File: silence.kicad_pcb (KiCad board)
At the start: 2 copper layers, 134 parts, among them J1 15EDGVC-3.81-02P, J2 15EDGVC-2.5-04P-14, J3 DEBUG, J4 15EDGVC-3.81-03P, J5 15EDGVC-3.81-02P, J6 EXTRA, J7 15EDGVC-3.81-03P, Q1 AO3400A, Q2 AO3400A, Q3 AO3400A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

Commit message: Minor updates
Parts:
- removed C13, C14, C15, C16, C17, C18, C19: 10u, Capacitor_SMD:C_1206_3216Metric
- added C6: 100u (EEEFTH101XAP), Capacitor_SMD:CP_Elec_6.3x7.7, F.Cu at (196.5, 62.7)
- added R47: 0, Resistor_SMD:R_0603_1608Metric, F.Cu at (213.0, 116.7)
- moved C21 345.3 mm to (276.2, 77.1)
- moved C23 345.3 mm to (276.2, 79.6)
- moved C24 345.3 mm to (276.2, 82.1)
- moved J6 345.3 mm to (279.9, 87.1)
- moved R26 345.3 mm to (276.2, 84.6)
- moved R27 345.3 mm to (276.2, 87.1)
- moved C22 345.3 mm to (285.7, 77.5)
- moved J3 345.3 mm to (280.6, 78.2)
- moved JP1 345.3 mm to (285.7, 81.0)
- moved SW1 345.3 mm to (265.7, 77.9)
- moved SW2 345.3 mm to (265.7, 86.4)
- moved U1 345.3 mm to (288.2, 64.8)
- moved C1 200.4 mm to (42.0, 22.8)
- moved C2 200.4 mm to (42.0, 25.3)
- moved C3 200.4 mm to (42.0, 27.8)
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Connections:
- FB2 pad 1: Net-(U8--) -> Net-(FB2-Pad1)
- R41 pad 1: Net-(U8-+) -> Net-(R41-Pad1)
- R41 pad 2: Net-(R41-Pad2) -> GND
- R42 pad 1: Net-(R41-Pad2) -> Net-(U8-+)
- R42 pad 2: GND -> Net-(R41-Pad1)
- U8 pad 4: Net-(U8--) -> Net-(FB2-Pad1)

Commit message: Routing almost finished
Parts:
- added C13: 10u, Capacitor_SMD:C_1206_3216Metric, F.Cu at (153.9, 66.0)
- added C14: 47u, Capacitor_SMD:C_1206_3216Metric, F.Cu at (153.9, 68.4)
- added D3: LED, LED_SMD:LED_0603_1608Metric, F.Cu at (173.1, 84.5)
- added D4: LED, LED_SMD:LED_0603_1608Metric, F.Cu at (173.1, 86.1)
- added D5: LED, LED_SMD:LED_0603_1608Metric, F.Cu at (166.3, 54.1)
- added JP3: WSEN, Jumper:SolderJumper-2_P1.3mm_Open_RoundedPad1.0x1.5mm, F.Cu at (191.9, 90.7)
- added JP4: WSEN, Jumper:SolderJumper-2_P1.3mm_Open_RoundedPad1.0x1.5mm, F.Cu at (191.9, 74.8)
- added L4: 4.7uH (SWPA5020S4R7MT), Inductor_SMD:L_Sunlord_SWPA5020S, F.Cu at (154.7, 62.0)
- added R48: 330, Resistor_SMD:R_0603_1608Metric, F.Cu at (153.1, 104.9)
- added R49: 330, Resistor_SMD:R_0603_1608Metric, F.Cu at (153.1, 101.9)
- added R50: 1, Resistor_SMD:R_0603_1608Metric, F.Cu at (150.8, 67.7)
- added R51: 10k, Resistor_SMD:R_0603_1608Metric, F.Cu at (170.0, 84.5)
- added R52: 10k, Resistor_SMD:R_0603_1608Metric, F.Cu at (170.0, 86.1)
- added R53: 47k, Resistor_SMD:R_0603_1608Metric, F.Cu at (163.3, 54.1)
- added kibuzzard-676F239E: G***, kibuzzard-676F239E, F.Cu at (149.9, 56.4)
- added kibuzzard-676F239E: G***, kibuzzard-676F239E, F.Cu at (199.8, 48.0)
- added kibuzzard-676F2404: G***, kibuzzard-676F2404, F.Cu at (149.9, 60.3)
- added kibuzzard-676F2404: G***, kibuzzard-676F2404, F.Cu at (201.0, 68.6)
- added kibuzzard-676F2425: G***, kibuzzard-676F2425, F.Cu at (150.5, 49.4)
- added kibuzzard-676F243D: G***, kibuzzard-676F243D, F.Cu at (195.7, 44.0)
- added kibuzzard-676F24DA: G***, kibuzzard-676F24DA, F.Cu at (203.6, 85.2)
- added kibuzzard-676F24FA: G***, kibuzzard-676F24FA, F.Cu at (197.6, 101.1)
- added kibuzzard-676F26EA: G***, kibuzzard-676F26EA, F.Cu at (161.0, 73.1)
- J6: footprint Connector_PinHeader_1.00mm:PinHeader_1x05_P1.00mm_Vertical -> Connector_PinHeader_2.54mm:PinHeader_1x05_P2.54mm_Vertical
- TP1, TP3: value DIN -> DO
- moved H3 245.9 mm to (203.9, 104.5)
- moved H1 225.6 mm to (203.9, 44.5)
- moved H4 192.5 mm to (143.9, 104.5)
- moved J2 174.8 mm to (150.7, 74.6), turned to 180 degrees
- moved H2 167.9 mm to (143.9, 44.5)
- moved J1 167.6 mm to (144.2, 56.4), turned to -90 degrees
- moved R8 161.8 mm to (188.9, 101.1)
- moved C1 161.3 mm to (185.0, 97.4), turned to 90 degrees
- moved C4 161.2 mm to (188.9, 96.7), turned to 180 degrees
- moved C3 158.4 mm to (182.5, 101.0)
- moved R45 158.4 mm to (189.6, 102.6), turned to 180 degrees
- moved C2 156.2 mm to (181.0, 96.5)
- moved R39 155.7 mm to (185.0, 100.4), turned to 90 degrees
- moved R6 154.7 mm to (179.4, 101.1)
- moved U3 154.4 mm to (188.9, 98.9)
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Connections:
- C28 pad 2: Net-(C28-Pad2) -> /Internal Power/SW
- C29 pad 1: +3V3 -> /Internal Power/3V3_UNFILT
- C30 pad 1: +3V3 -> /Internal Power/3V3_UNFILT
- C31 pad 1: Net-(C28-Pad2) -> /Internal Power/3V3_UNFILT
- L2 pad 1: Net-(C28-Pad2) -> /Internal Power/SW
- L2 pad 2: +3V3 -> /Internal Power/3V3_UNFILT
- R12 pad 1: +VDC -> Net-(JP4-A)
- R15 pad 1: +VDC -> Net-(JP4-A)
- R18 pad 1: +VDC -> Net-(JP3-A)
- R20 pad 1: +VDC -> Net-(JP3-A)
- R29 pad 1: Net-(C28-Pad2) -> /Internal Power/3V3_UNFILT
- U1 pad 14: unconnected-(U1-IO12-Pad14) -> /ESP/LED_A
- U1 pad 16: unconnected-(U1-IO13-Pad16) -> /ESP/LED_B
- U1 pad 34: Net-(J3-Pin_2) -> Net-(U1-RXD0/IO3)
- U1 pad 35: Net-(J3-Pin_1) -> Net-(U1-TXD0/IO1)
- U6 pad 1: Net-(C28-Pad2) -> /Internal Power/SW
- U6 pad 2: Net-(C28-Pad2) -> /Internal Power/SW
- U6 pad 3: Net-(C28-Pad2) -> /Internal Power/SW
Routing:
- net /SENS: track 0.00 -> 104.7 mm, vias 0 -> 5
- net GND: track 0.00 -> 87.8 mm, vias 0 -> 254
- net /SET: track 0.00 -> 85.4 mm, vias 0 -> 3
- net /EN: track 0.00 -> 80.6 mm, vias 0 -> 2
- net +VDC: track 0.00 -> 77.2 mm, vias 0 -> 80
- net VOFF: track 0.00 -> 75.1 mm, vias 0 -> 4
- net /ESP/WS_A: track 0.00 -> 52.1 mm, vias 0 -> 2
- net /ESP/WS_B: track 0.00 -> 48.5 mm, vias 0 -> 2
- net /ESP/EN: track 0.00 -> 40.5 mm, vias 0 -> 2
- net +3V3: track 0.00 -> 34.5 mm, vias 0 -> 30
- net /Current Sense/V_{In}: track 0.00 -> 23.9 mm, vias 0 -> 2
- net /ESP/IO0: track 0.00 -> 20.2 mm
- net /Internal Power/3V3_UNFILT: track 0.00 -> 16.9 mm, vias 0 -> 2
- net /ESP/DAC_2: track 0.00 -> 15.3 mm, vias 0 -> 2
- net Net-(JP4-A): track 0.00 -> 12.5 mm, vias 0 -> 2
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- added copper zone on F.Cu, net +3V3
- added copper zone on In2.Cu, net +3V3
- added copper zone on B.Cu, net +VDC
- added copper zone on F.Cu, net +VDC
- added copper zone on F.Cu, net /Current Sense/V_{In}
- added copper zone on F.Cu, net /Current Sense/V_{out}
- added copper zone on F.Cu, net /DCDC/SW
- added copper zone on F.Cu, net /Internal Power/3V3_UNFILT
- added copper zone on F.Cu, net /Internal Power/SW
- added copper zone on B.Cu, net GND
- added copper zone on F.Cu, net GND
- added copper zone on In1.Cu, net GND
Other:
- board outline added: 68 x 68 mm
- copper layers 2 -> 4
- board text added: "+ D G"
- board text added: "2 4 5 18 G"
- board text added: "3V3"
- board text added: "G R T"
- board text added: "GND EN SET SNS"
- board text added: "IMAX"
- board text added: "IO12"
- board text added: "IO13"
- board text added: "Max 28V and 5A"
- board text added: "V_{IN}"
- board text added: "ZERO"
- board text added: "by atx"
- board text added: "{gitCommit}"
- board text added: "{gitDate}"
- board text added: "~{EN}"
- board text added: "~{IO0}"

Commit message: Minor updates
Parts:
- removed JP3, JP4: WSEN, Jumper:SolderJumper-2_P1.3mm_Open_RoundedPad1.0x1.5mm
- removed Q2, Q4: AO3400A, Package_TO_SOT_SMD:SOT-23
- removed R13, R14, R17, R19: 1M, Resistor_SMD:R_0603_1608Metric
- added Q5: MMBT5551L, Package_TO_SOT_SMD:SOT-23, F.Cu at (193.9, 95.9)
- added Q6: MMBT5551L, Package_TO_SOT_SMD:SOT-23, F.Cu at (193.9, 80.0)
- added R54: 10k, Resistor_SMD:R_0603_1608Metric, F.Cu at (193.6, 98.7)
- added R55: 10k, Resistor_SMD:R_0603_1608Metric, F.Cu at (193.6, 82.8)
- Q1, Q3: value AO3400A -> MMBT5551L
- moved Q1 17.5 mm to (197.3, 95.9)
- moved Q3 14.3 mm to (197.3, 80.0)
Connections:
- Q1 pad 1: /ESP/WS_A -> Net-(Q1-B)
- Q1 pad 3: Net-(Q1-D) -> Net-(Q1-C)
- Q3 pad 1: /ESP/WS_B -> Net-(Q3-B)
- Q3 pad 3: Net-(Q3-D) -> Net-(Q3-C)
- R12 pad 1: Net-(JP4-A) -> +VDC
- R12 pad 2: Net-(Q1-D) -> Net-(Q3-B)
- R15 pad 1: Net-(JP4-A) -> +VDC
- R15 pad 2: Net-(Q2-D) -> Net-(Q3-C)
- R16 pad 1: Net-(Q2-D) -> Net-(Q3-C)
- R18 pad 1: Net-(JP3-A) -> +VDC
- R18 pad 2: Net-(Q3-D) -> Net-(Q1-B)
- R20 pad 1: Net-(JP3-A) -> +VDC
- R20 pad 2: Net-(Q4-D) -> Net-(Q1-C)
- R21 pad 1: Net-(Q4-D) -> Net-(Q1-C)
- R36 pad 1: Net-(Q4-D) -> Net-(Q1-C)
- R37 pad 1: Net-(Q2-D) -> Net-(Q3-C)
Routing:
- net Net-(Q1-C): track 0.00 -> 12.9 mm, vias 0 -> 2
- net Net-(JP4-A): track 12.5 -> 0.00 mm, vias 2 -> 0
- net Net-(JP3-A): track 12.5 -> 0.00 mm, vias 2 -> 0
- net Net-(Q1-B): track 0.00 -> 11.7 mm
- net Net-(Q3-B): track 0.00 -> 9.19 mm
- net Net-(Q1-D): track 8.85 -> 0.00 mm
- net Net-(Q3-D): track 8.85 -> 0.00 mm
- net Net-(Q3-C): track 0.00 -> 8.63 mm, vias 0 -> 2
- net Net-(J4-Pin_2): track 7.97 -> 15.9 mm
- net Net-(Q2-D): track 5.84 -> 0.00 mm
- net Net-(Q4-D): track 5.84 -> 0.00 mm
- net GND: track 87.8 -> 82.1 mm, vias 254 -> 278
- net +VDC: track 77.2 -> 81.2 mm, vias 80 -> 83
- net Net-(Q6-B): track 0.00 -> 1.83 mm
- net Net-(Q5-B): track 0.00 -> 1.83 mm
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
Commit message: Minor edits
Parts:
- added TP12: VDC, meteopress_footprints:TestPoint_THTPad_D2.0mm_Drill1.0mm, F.Cu at (161.6, 49.7)
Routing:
- net GND: vias 278 -> 284
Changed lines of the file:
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@@
 		(tags "resistor")
 		(property "Reference" "R55"
-			(at 0 -1.43 360)
+			(at 0 -1.43 0)
 			(layer "F.SilkS")
 			(hide yes)
@@
 		)
 		(property "Value" "10k"
-			(at 0 1.43 360)
+			(at 0 1.43 0)
 			(layer "F.Fab")
 			(effects
@@
 		)
 		(fp_text user "${REFERENCE}"
-			(at 0 0 360)
+			(at 0 0 0)
 			(layer "F.Fab")
 			(effects
@@
 			(at 0 -4.35 90)
 			(layer "F.SilkS")
+			(hide yes)
 			(effects
 				(font
@@
 		)
 		(fp_line
-			(start -4.4375 -1.8475)
-			(end -3.65 -1.8475)
+			(start -4.4375 1.7)
+			(end -3.65 1.7)
 			(stroke
 				(width 0.12)
@@
 		)
 		(fp_line
-			(start -4.04375 -2.24125)
-			(end -4.04375 -1.45375)
+			(start -4.04375 1.30625)
+			(end -4.04375 2.09375)
 			(stroke
 				(width 0.12)
@@
 		)
 	)
+	(footprint "meteopress_footprints:TestPoint_THTPad_D2.0mm_Drill1.0mm"
+		(layer "F.Cu")
+		(at 161.6 49.7)
+		(descr "THT pad as test Point, diameter 2.0mm, hole diameter 1.0mm")
+		(tags "test point THT pad")
+		(property "Reference" "TP12"
+			(at 0 -1.998 0)
+			(layer "F.Fab")
+			(effects
+				(font
+					(size 1 1)
+					(thickness 0.15)
+				)
+			)
+		)
+		(property "Value" "VDC"
+			(at 2.8 0 0)
+			(layer "F.SilkS" knockout)
+			(effects
+				(font
+					(size 1 1)
+					(thickness 0.2)
+				)
+			)
+		)
+		(property "Footprint" "meteopress_footprints:TestPoint_THTPad_D2.0mm_Drill1.0mm"
+			(at 0 0 0)
+			(layer "F.Fab")
+			(hide yes)
+			(effects
+				(font
+					(size 1.27 1.27)
+					(thickness 0.15)
+				)
+			)
+		)
+		(property "Datasheet" ""
+			(at 0 0 0)
+			(layer "F.Fab")
+			(hide yes)
+			(effects
+				(font
+					(size 1.27 1.27)
+					(thickness 0.15)
+				)
+			)
+		)
+		(property "Description" "test point"
+			(at 0 0 0)
+			(layer "F.Fab")
+			(hide yes)
+			(effects
+				(font
+					(size 1.27 1.27)
+					(thickness 0.15)
+				)
+			)
+		)
+		(property "LCSC" "C5199804"
+			(at 0 0 0)
+			(unlocked yes)
+			(layer "F.Fab")
+			(hide yes)
+			(effects
+				(font
+					(size 1 1)
+					(thickness 0.15)
+				)
+			)
+		)
+		(property ki_fp_filters "Pin* Test*")
+		(sheetname "Root")
+		(sheetfile "silence.kicad_sch")
+		(fp_circle
+			(center 0 0)
+			(end 0 1.2)
+			(stroke
+				(width 0.12)
+				(type solid)
+			)
+			(fill none)
+			(layer "F.SilkS")
+		)
+		(fp_circle
+			(center 0 0)
+			(end 1.5 0)
+			(stroke
+				(width 0.05)
+				(type solid)
+			)
+			(fill none)
+			(layer "F.CrtYd")
+		)
+		(pad "1" thru_hole circle
+			(at 0 0)
+			(size 2 2)
+			(drill 1)
+			(layers "*.Cu" "*.Mask")
+			(remove_unused_layers no)
+			(net 7 "+VDC")
+			(pinfunction "1")
+			(pintype "passive")
+		)
+	)
 	(footprint "meteopress_footprints:15EDGVC-2.5-04P-14"
 		(layer "F.Cu")
@@
 		(tags "resistor")
 		(property "Reference" "R54"
-			(at 0 -1.43 360)
+			(at 0 -1.43 0)
 			(layer "F.SilkS")
 			(hide yes)
@@
 		)
 		(property "Value" "10k"
-			(at 0 1.43 360)
+			(at 0 1.43 0)
 			(layer "F.Fab")
 			(effects
@@
 		)
 		(fp_text user "${REFERENCE}"
-			(at 0 0 360)
+			(at 0 0 0)
 			(layer "F.Fab")
 			(effects
@@
 	)
 	(via
+		(at 161.5 77.7)
+		(size 0.6)
+		(drill 0.3)
+		(layers "F.Cu" "B.Cu")
+		(free yes)
+		(net 1)
+	)
+	(via
 		(at 179.8 87.3)
 		(size 1)
@@
 	)
 	(via
+		(at 155 77.7)
+		(size 0.6)
+		(drill 0.3)
+		(layers "F.Cu" "B.Cu")
+		(free yes)
+		(net 1)
+	)
+	(via
 		(at 188.1 95.8)
 		(size 0.6)
@@
 	)
 	(via
+		(at 164.7 77.7)
+		(size 0.6)
+		(drill 0.3)
+		(layers "F.Cu" "B.Cu")
+		(free yes)
+		(net 1)
+	)
+	(via
 		(at 168.5 90.5)
 		(size 1)
@@
 	)
 	(via
-		(at 159.6 79.1)
+		(at 159.7 79.6)
 		(size 0.6)
 		(drill 0.3)
@@
 	)
 	(via
+		(at 158.3 77.7)
+		(size 0.6)
+		(drill 0.3)
+		(layers "F.Cu" "B.Cu")
+		(free yes)
+		(net 1)
+	)
+	(via
 		(at 159.8 72.8)
 		(size 1)
@@
 	)
 	(via
+		(at 167.5 79.9)
+		(size 0.6)
+		(drill 0.3)
+		(layers "F.Cu" "B.Cu")
+		(free yes)
+		(net 1)
+	)
+	(via
 		(at 148.1 101.8)
 		(size 1)
@@
 	)
 	(via
-		(at 165.9 76.7)
+		(at 166.2 75.4)
 		(size 0.6)
 		(drill 0.3)
@@
 	)
 	(via
-		(at 162.7 79.2)
+		(at 162.7 79.5)
 		(size 0.6)
 		(drill 0.3)
@@
 	)
 	(via
-		(at 155.387405 76.878981)
+		(at 155.5 75.4)
 		(size 0.6)
 		(drill 0.3)
@@
 	)
 	(via
-		(at 155.2 79.1)
+		(at 155.2 79.6)
 		(size 0.6)
 		(drill 0.3)
@@
 	)
 	(via
-		(at 165.2 79.1)
+		(at 165.3 79.7)
 		(size 0.6)
 		(drill 0.3)
@@
 	)
 	(via
+		(at 166.9 77.7)
+		(size 0.6)
+		(drill 0.3)
+		(layers "F.Cu" "B.Cu")
+		(free yes)
+		(net 1)
+	)
+	(via
 		(at 164.9 75.2)
 		(size 1)
@@
 	)
 	(via
-		(at 157.5 79.2)
+		(at 157.6 79.7)
 		(size 0.6)
 		(drill 0.3)
@@
 	)
 	(via
-		(at 151.2 77.7)
+		(at 151.5 77.4)
 		(size 0.6)
 		(drill 0.3)
@@
 	)
 	(via
-		(at 158.8 47.8)
+		(at 158 47.9)
 		(size 1)
 		(drill 0.5)
@@
 	)
 	(segment
-		(start 168 77.6)
-		(end 169.9 79.5)
-		(width 0.2)
-		(layer "B.Cu")
-		(net 29)
-	)
-	(segment
 		(start 197.6 51.18)
 		(end 196.6 50.18)
@@
 	)
 	(segment
-		(start 153.7 77.6)
-		(end 168 77.6)
+		(start 167.3 76.9)
+		(end 169.9 79.5)
 		(width 0.2)
 		(layer "B.Cu")
@@
 	)
 	(segment
+		(start 150.7 74.6)
+		(end 153 76.9)
+		(width 0.2)
+		(layer "B.Cu")
+		(net 29)
+	)
+	(segment
 		(start 169.9 95.8)
 		(end 169.9 93.9)
@@
 	)
 	(segment
-		(start 150.7 74.6)
-		(end 153.7 77.6)
+		(start 153 76.9)
+		(end 167.3 76.9)
 		(width 0.2)
 		(layer "B.Cu")
@@
 				(xy 140.4 57.8) (xy 150.9 57.4) (xy 162 60.1) (xy 163.7 60.1) (xy 164 62.5) (xy 165.5 62.5) (xy 166.113423 59.490604)
 				(xy 174.7 58.8) (xy 175.769942 60.304624) (xy 176.6 65.7) (xy 183.6 65.7) (xy 183.6 61.7) (xy 186.4 60)
-				(xy 186.4 41.4) (xy 150.4 41.4) (xy 142.7 52) (xy 140.2 52)
+				(xy 189 58.8) (xy 186.4 55.3) (xy 186.4 41.4) (xy 150.4 41.4) (xy 142.7 52) (xy 140.2 52)
 			)
 		)

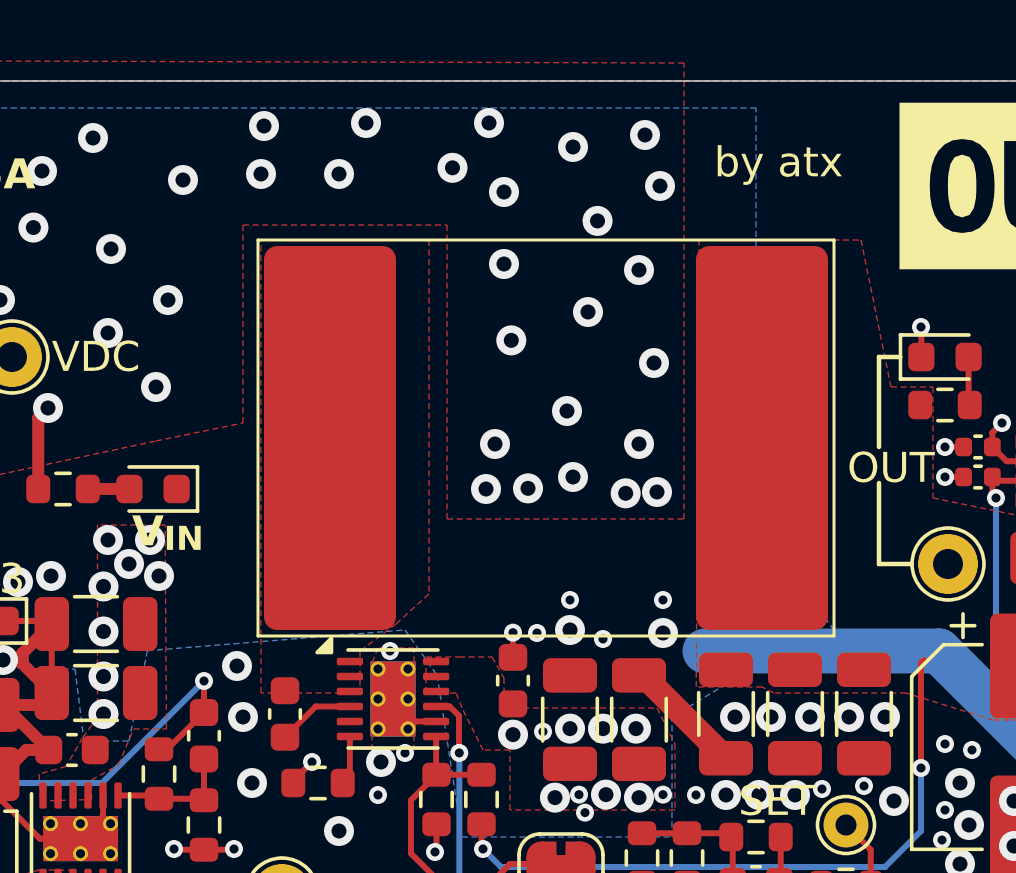
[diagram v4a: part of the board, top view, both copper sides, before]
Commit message: Manufacturing update + inductor fix
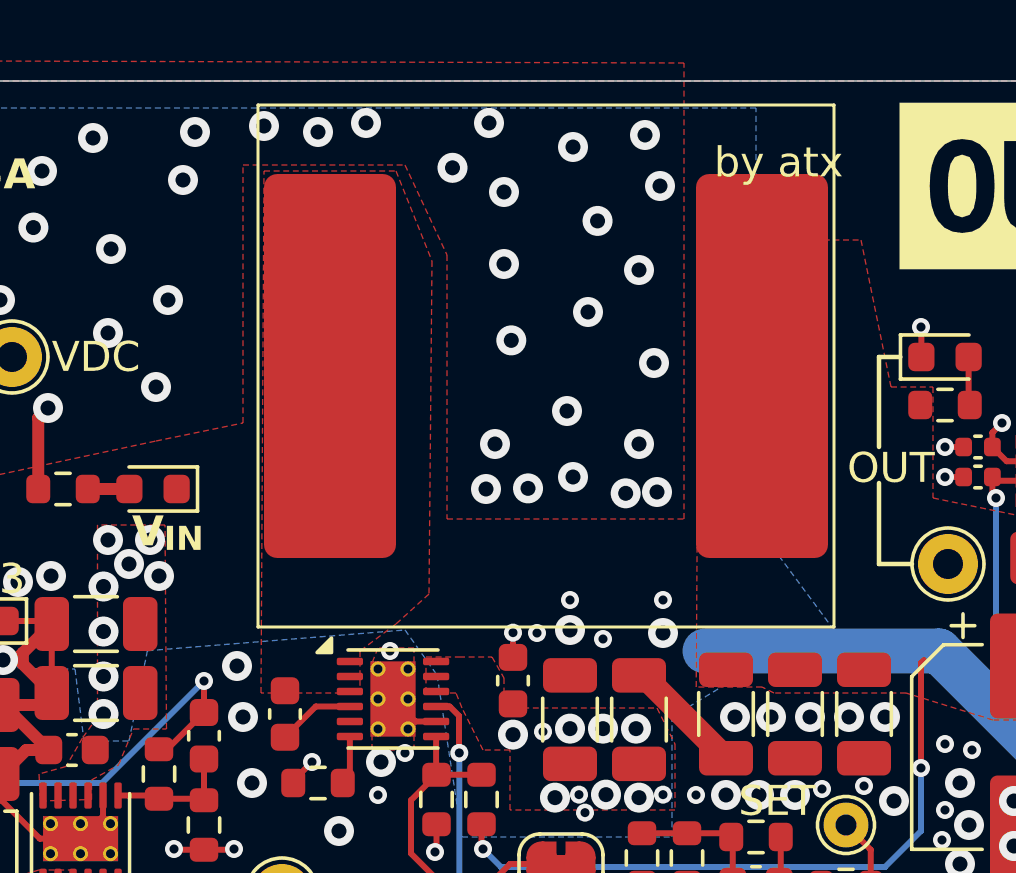
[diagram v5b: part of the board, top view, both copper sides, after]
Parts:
- moved L1 2.40 mm to (179.4, 50.0)
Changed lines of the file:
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@@
 	(footprint "footprints:YSPIA1770"
 		(layer "F.Cu")
-		(at 179.4 52.4)
+		(at 179.4 50)
 		(property "Reference" "L1"
 			(at 0 -0.5 0)
@@
 		(attr smd)
 		(fp_line
-			(start -9.6 -6.6)
-			(end 9.6 -6.6)
+			(start -9.6 -8.7)
+			(end 9.6 -8.7)
 			(stroke
 				(width 0.1)
@@
 		)
 		(fp_line
-			(start -9.6 6.6)
-			(end -9.6 -6.6)
+			(start -9.6 8.7)
+			(end -9.6 -8.7)
 			(stroke
 				(width 0.1)
@@
 		)
 		(fp_line
-			(start 9.6 -6.6)
-			(end 9.6 6.6)
+			(start -9.6 8.7)
+			(end 9.6 8.7)
 			(stroke
 				(width 0.1)
@@
 		)
 		(fp_line
-			(start 9.6 6.6)
-			(end -9.6 6.6)
+			(start 9.6 -8.7)
+			(end 9.6 8.7)
 			(stroke
 				(width 0.1)
@@
 		)
 		(fp_line
-			(start -9.6 -6.6)
-			(end 9.6 -6.6)
+			(start -9.6 -8.7)
+			(end 9.6 -8.7)
 			(stroke
 				(width 0.05)
@@
 		)
 		(fp_line
-			(start -9.6 6.6)
-			(end -9.6 -6.6)
+			(start -9.6 8.7)
+			(end -9.6 -8.7)
 			(stroke
 				(width 0.05)
@@
 		)
 		(fp_line
-			(start 9.6 -6.6)
-			(end 9.6 6.6)
+			(start 9.6 -8.7)
+			(end 9.6 8.7)
 			(stroke
 				(width 0.05)
@@
 		)
 		(fp_line
-			(start 9.6 6.6)
-			(end -9.6 6.6)
+			(start 9.6 8.7)
+			(end -9.6 8.7)
 			(stroke
 				(width 0.05)
@@
 	)
 	(via
-		(at 169.9 43.6)
+		(at 167.7 42.2)
 		(size 1)
 		(drill 0.5)
@@
 	)
 	(via
-		(at 172.5 43.6)
+		(at 171.8 42.2)
 		(size 1)
 		(drill 0.5)
@@
 		(polygon
 			(pts
-				(xy 140.3 58.4) (xy 147.6 58.4) (xy 149.6 56.1) (xy 166.4 52.5) (xy 169.3 51.9) (xy 169.3 45.3)
-				(xy 176.1 45.3) (xy 176.1 55.1) (xy 184 55.1) (xy 184 39.9) (xy 148.9 39.8) (xy 147.5 46) (xy 145.2 48.4)
-				(xy 140.3 50)
+				(xy 140.3 58.4) (xy 147.6 58.4) (xy 149.6 56.1) (xy 166.4 52.5) (xy 169.3 51.9) (xy 169.3 43.3)
+				(xy 174.7 43.3) (xy 176.1 46.3) (xy 176.1 55.1) (xy 184 55.1) (xy 184 39.9) (xy 148.9 39.8) (xy 147.5 46)
+				(xy 145.2 48.4) (xy 140.3 50)
 			)
 		)
@@
 		(polygon
 			(pts
-				(xy 173.2 60.9) (xy 169.9 60.9) (xy 169.9 45.8) (xy 175.5 45.8) (xy 175.5 57.6) (xy 174.4 58.6)
+				(xy 173.2 60.9) (xy 169.9 60.9) (xy 170 43.5) (xy 174.4 43.5) (xy 175.6 46.5) (xy 175.5 57.6) (xy 174.4 58.6)
 				(xy 173.2 59.5)
 			)
